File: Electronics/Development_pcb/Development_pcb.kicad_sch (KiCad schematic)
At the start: 11 parts, among them J1 TF-Luna, J2 Pan, J3 Tilt, J4 MP3, Q1 NPN, U1 ESP32-S3-DEVKIT:C-1-N16R8, U2 MP3-TF-16P

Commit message: Refactor code structure for improved readability and maintainability
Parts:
- added D1: 1N5822, Diode_THT:D_DO-201AD_P15.24mm_Horizontal, symbol Diode:1N5822
- added J5: Display, symbol Connector:Conn_01x08_Pin
- added J6: LAZER, symbol Connector:Conn_01x02_Pin
- added J7: Screw_Terminal_01x02, symbol Connector:Screw_Terminal_01x02
- Q1: value NPN -> 2N2222A
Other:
- moved on the sheet: C1, C2, R1, R2

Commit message: Refactor code structure for improved readability and maintainability
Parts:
- removed D1: 1N5822, Diode_THT:D_DO-201AD_P15.24mm_Horizontal, symbol Diode:1N5822
- removed J7: Screw_Terminal_01x02, symbol Connector:Screw_Terminal_01x02
- added SW1: SW_SPST, Connector_PinHeader_2.54mm:PinHeader_1x02_P2.54mm_Vertical, symbol Switch:SW_SPST
- C1, C2: footprint (none) -> Capacitor_THT:CP_Radial_D10.0mm_P5.00mm
- J1: footprint (none) -> Connector_PinHeader_2.54mm:PinHeader_1x04_P2.54mm_Vertical
- J2, J3: footprint (none) -> Connector_PinHeader_2.54mm:PinHeader_1x03_P2.54mm_Vertical
- J4, J6: footprint (none) -> Connector_PinHeader_2.54mm:PinHeader_1x02_P2.54mm_Vertical
- J5: footprint (none) -> Connector_PinHeader_2.54mm:PinHeader_1x08_P2.54mm_Vertical
- Q1: footprint (none) -> Package_TO_SOT_THT:TO-92_Inline
- R1, R2: footprint (none) -> Resistor_THT:R_Axial_DIN0207_L6.3mm_D2.5mm_P7.62mm_Horizontal
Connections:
- net +5V: now also C1.1, C2.1, J1.4 (Pin_4), J2.2 (Pin_2), J3.2 (Pin_2), U1.J1_21 (5V0), U2.P$1 (VCC), SW1.2 (B)
- net GND: now also C1.2, C2.2, J1.1 (Pin_1), J2.3 (Pin_3), J3.1 (Pin_1), J5.1 (Pin_1), Q1.3 (E), U1.J3_1 (GND), U2.P$10 (GND2)
- net at Q1.1 (C): now also J6.1 (Pin_1)
- net at Q1.2 (B): now also R1.1
- net at R1.2: now also U1.J1_6 (GPIO6)
- net +3.3V: now reaches J5.2 (Pin_2)
- net +3.3V: now also J5.8 (Pin_8)
- net at J5.3 (Pin_3): now also U1.J1_8 (GPIO15)
- net at J5.4 (Pin_4): now also U1.J1_15 (GPIO9)
- net at J5.5 (Pin_5): now also U1.J1_16 (GPIO10)
- net at J5.6 (Pin_6): now also U1.J1_17 (GPIO11)
- net at J5.7 (Pin_7): now also U1.J1_18 (GPIO12)
- net at J2.1 (Pin_1): now also U1.J1_4 (GPIO4)
- net at J4.1 (Pin_1): now also U2.P$6 (SPK2)
- net at J4.2 (Pin_2): now also U2.P$8 (SPK1)
- net at U2.P$2 (RX): now also R2.1
- net at U2.P$3 (TX): now also U1.J1_19 (GPIO13)
- net at J6.2 (Pin_2): now also SW1.1 (A)
- net at U1.J1_10 (GPIO17): now also J1.2 (Pin_2)
- net at U1.J1_11 (GPIO18): now also J1.3 (Pin_3)
- net at U1.J1_20 (GPIO14): now also R2.2
- net at U1.J1_5 (GPIO5): now also J3.3 (Pin_3)
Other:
- company: (none) -> Artyom Kiselhof
- title: (none) -> MISA_PCB
- moved on the sheet: C1, C2, R1, R2

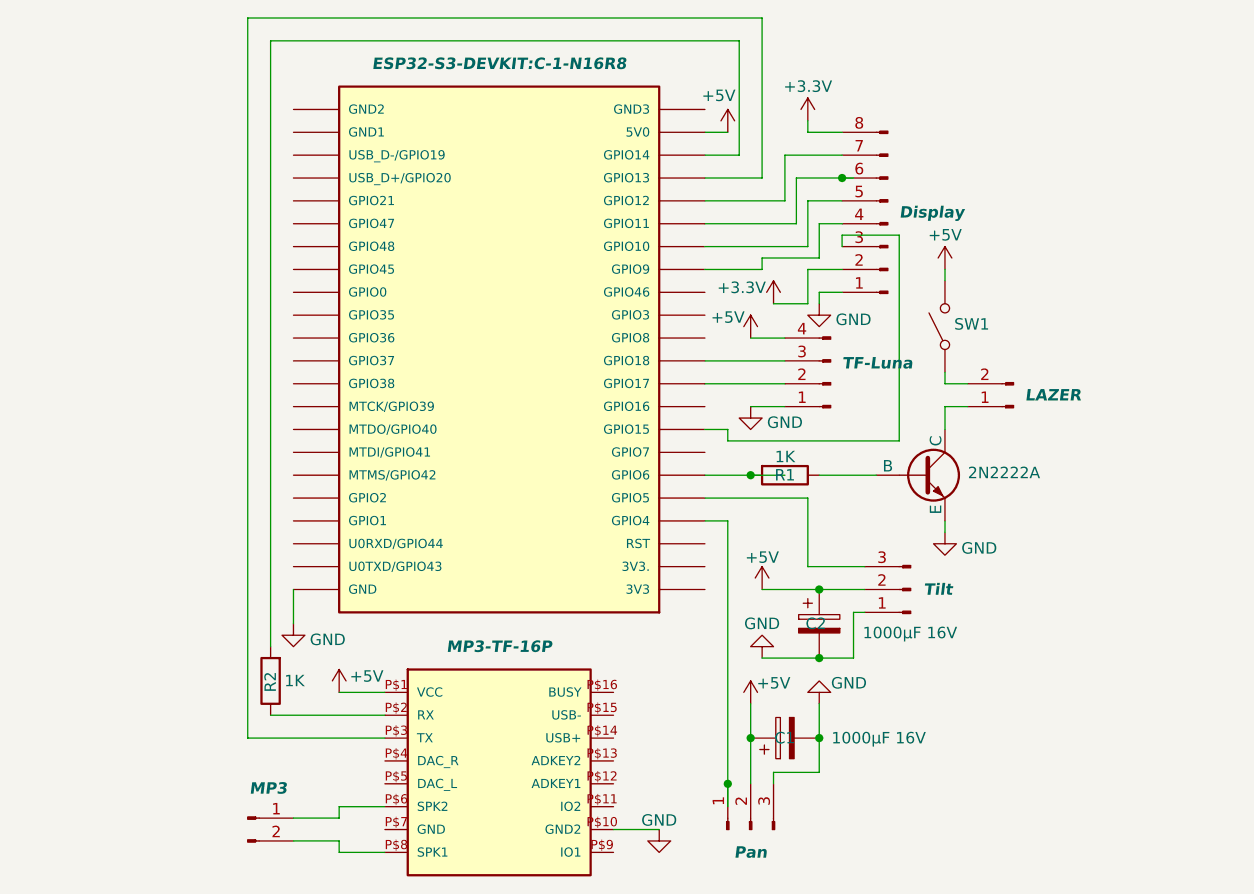
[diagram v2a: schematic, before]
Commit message: Add .DS_Store files and ERC report for Development PCB
- Created .DS_Store files in Electronics and Electronics/Development_pcb directories to store custom Finder attributes.
- Added ERC report (ERC.rpt) for the Development PCB, highlighting errors related to unconnected power pins and pin type mismatches.
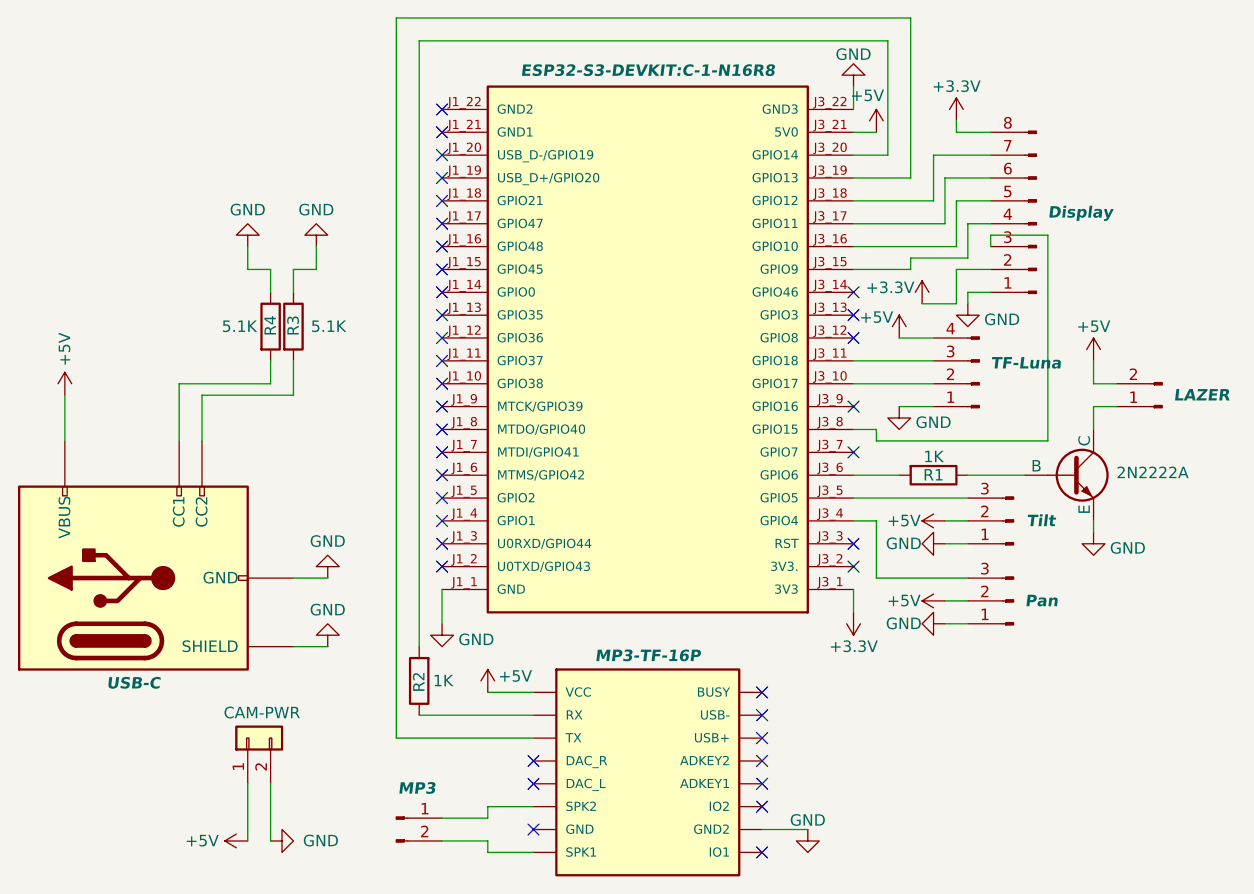
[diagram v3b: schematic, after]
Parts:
- removed C1, C2: 1000µF 16V, Capacitor_THT:CP_Radial_D10.0mm_P5.00mm, symbol Device:C_Polarized
- removed SW1: SW_SPST, Connector_PinHeader_2.54mm:PinHeader_1x02_P2.54mm_Vertical, symbol Switch:SW_SPST
- added J7: CAM-PWR, Connector_PinHeader_2.54mm:PinHeader_1x02_P2.54mm_Vertical, symbol Connector_Generic:Conn_01x02
- added J8: USB-C, Connector_USB:USB_C_Receptacle_HRO_TYPE-C-31-M-12, symbol Connector:USB_C_Receptacle_PowerOnly_6P
- added R3, R4: 5.1K, Resistor_THT:R_Axial_DIN0207_L6.3mm_D2.5mm_P7.62mm_Horizontal, symbol Device:R
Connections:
- net +3.3V: now also U1.J3_1 (3V3)
- net +5V: now also J6.2 (Pin_2), U1.J3_21 (5V0), J7.1 (Pin_1), J8.A9 (VBUS), J8.B9 (VBUS); no longer U1.J1_21 (5V0)
- net GND: now also J2.1 (Pin_1), U1.J1_1 (GND), U1.J3_22 (GND3), J7.2 (Pin_2), J8.A12 (GND), J8.B12 (GND), J8.SH (SHIELD), R3.1, R4.1; no longer J2.3 (Pin_3), U1.J3_1 (GND)
- net at R1.2: now also U1.J3_6 (GPIO6); no longer U1.J1_6 (GPIO6)
- net at J5.3 (Pin_3): now also U1.J3_8 (GPIO15); no longer U1.J1_8 (GPIO15)
- net at J5.4 (Pin_4): now also U1.J3_15 (GPIO9); no longer U1.J1_15 (GPIO9)
- net at J5.5 (Pin_5): now also U1.J3_16 (GPIO10); no longer U1.J1_16 (GPIO10)
- net at J5.6 (Pin_6): now also U1.J3_17 (GPIO11); no longer U1.J1_17 (GPIO11)
- net at J5.7 (Pin_7): now also U1.J3_18 (GPIO12); no longer U1.J1_18 (GPIO12)
- net at U1.J1_4 (GPIO1): no longer J2.1 (Pin_1)
- net at U2.P$3 (TX): now also U1.J3_19 (GPIO13); no longer U1.J1_19 (GPIO13)
- net at U1.J1_10 (GPIO38): no longer J1.2 (Pin_2)
- net at U1.J1_11 (GPIO37): no longer J1.3 (Pin_3)
- net at U1.J1_20 (USB_D-/GPIO19): no longer R2.2
- net at U1.J1_5 (GPIO2): no longer J3.3 (Pin_3)
- net at U1.J3_10 (GPIO17): now also J1.2 (Pin_2)
- net at U1.J3_11 (GPIO18): now also J1.3 (Pin_3)
- net at U1.J3_20 (GPIO14): now also R2.2
- net at U1.J3_4 (GPIO4): now also J2.3 (Pin_3)
- net at U1.J3_5 (GPIO5): now also J3.3 (Pin_3)
- new net: J8.A5 (CC1), R4.2
- new net: J8.B5 (CC2), R3.2
- no-connect marks 0 -> 38
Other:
- moved on the sheet: R1, R2

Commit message: changes
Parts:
- removed J1: TF-Luna, Connector_PinHeader_2.54mm:PinHeader_1x04_P2.54mm_Vertical, symbol Connector:Conn_01x04_Pin
- removed J2: Pan, Connector_PinHeader_2.54mm:PinHeader_1x03_P2.54mm_Vertical, symbol Connector:Conn_01x03_Pin
- removed J3: Tilt, Connector_PinHeader_2.54mm:PinHeader_1x03_P2.54mm_Vertical, symbol Connector:Conn_01x03_Pin
- removed J4: MP3, Connector_PinHeader_2.54mm:PinHeader_1x02_P2.54mm_Vertical, symbol Connector:Conn_01x02_Pin
- removed J5: Display, Connector_PinHeader_2.54mm:PinHeader_1x08_P2.54mm_Vertical, symbol Connector:Conn_01x08_Pin
- removed J6: LAZER, Connector_PinHeader_2.54mm:PinHeader_1x02_P2.54mm_Vertical, symbol Connector:Conn_01x02_Pin
- removed J7: CAM-PWR, Connector_PinHeader_2.54mm:PinHeader_1x02_P2.54mm_Vertical, symbol Connector_Generic:Conn_01x02
- removed J8: USB-C, Connector_USB:USB_C_Receptacle_HRO_TYPE-C-31-M-12, symbol Connector:USB_C_Receptacle_PowerOnly_6P
- removed Q1: 2N2222A, Package_TO_SOT_THT:TO-92_Inline, symbol Simulation_SPICE:NPN
- removed R1, R2: 1K, Resistor_THT:R_Axial_DIN0207_L6.3mm_D2.5mm_P7.62mm_Horizontal, symbol Device:R
- removed R3, R4: 5.1K, Resistor_THT:R_Axial_DIN0207_L6.3mm_D2.5mm_P7.62mm_Horizontal, symbol Device:R
- added C1: 1000µF, Capacitor_THT:CP_Radial_D10.0mm_P5.00mm, symbol Device:C_Polarized_Small
- added C2, C5: 100nF, Capacitor_THT:C_Disc_D5.0mm_W2.5mm_P5.00mm, symbol Device:C_Small
- added C3, C4: 470µF, Capacitor_THT:CP_Radial_D8.0mm_P3.50mm, symbol Device:C_Polarized_Small
- added D1: SA5.0A, Diode_THT:D_DO-15_P10.16mm_Horizontal, symbol Device:D_TVS_Small
- added D2: 1N5819, Diode_THT:D_DO-41_SOD81_P10.16mm_Horizontal, symbol Device:D_Schottky_Small
- added F1: Polyfuse, Capacitor_THT:C_Disc_D5.0mm_W2.5mm_P5.00mm, symbol Device:Polyfuse_Small
- added J1: Pan-Servo, Connector_PinHeader_2.54mm:PinHeader_1x03_P2.54mm_Vertical, symbol Connector_Generic:Conn_01x03
- added J2: Tilt-Servo, Connector_PinHeader_2.54mm:PinHeader_1x03_P2.54mm_Vertical, symbol Connector_Generic:Conn_01x03
- added J3: cam-power, Connector_JST:JST_XH_B2B-XH-A_1x02_P2.50mm_Vertical, symbol Connector_Generic:Conn_01x02
- added J4: laser-power, Connector_JST:JST_XH_B2B-XH-A_1x02_P2.50mm_Vertical, symbol Connector_Generic:Conn_01x02
- added J5: SPEAKER, Connector_JST:JST_XH_B2B-XH-A_1x02_P2.50mm_Vertical, symbol Connector_Generic:Conn_01x02
- added J6: TFT_display, Connector_JST:JST_XH_B8B-XH-A_1x08_P2.50mm_Vertical, symbol Connector_Generic:Conn_01x08
- added J7: lidar-TOF, Connector_PinHeader_2.54mm:PinHeader_1x04_P2.54mm_Vertical, symbol Connector_Generic:Conn_01x04
- added J8: USB_C_IN, TerminalBlock_Phoenix:TerminalBlock_Phoenix_MKDS-3-2-5.08_1x02_P5.08mm_Horizontal, symbol Connector:Screw_Terminal_01x02
- added Q1: PN2222A, Package_TO_SOT_THT:TO-92_Inline, symbol Transistor_BJT:Q_NPN_EBC
- added R3: 1k, Resistor_THT:R_Axial_DIN0207_L6.3mm_D2.5mm_P10.16mm_Horizontal, symbol Device:R_Small
- added R4: 1kΩ, Resistor_THT:R_Axial_DIN0207_L6.3mm_D2.5mm_P10.16mm_Horizontal, symbol Device:R_Small
- U1: value ESP32-S3-DEVKIT:C-1-N16R8 -> ESP32-S3-DEVKITC-1-N8R8; footprint ESP32-S3-DEVKITC-1-N8R8:ESP32-S3-DEVKITC-1-N8R8 -> Development_pcb:ESP32-S3-DevKitC-1_Socket; Description_1 The ESP32-S3-DEVKITC-1-N8R8 from Espressif Systems is a dev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 -> (none)
- U2: Description_1 MP3 player module data sheet -> (none)
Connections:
- net +3.3V is gone; now on net GND: U1.J3_1 (GND)
- net +5V: now also C1.1, C2.1, C3.1, C4.1, C5.1, D1.1 (A1), D2.2 (A), F1.2, J1.2 (Pin_2), J2.2 (Pin_2), J3.2 (Pin_2), J4.2 (Pin_2), J7.4 (Pin_4); no longer U1.J3_21 (5V0)
- net GND: now also U1.J1_22 (GND3), U1.J3_21 (GND1), U2.P$7 (GND), C1.2, C2.2, C3.2, C4.2, C5.2, D1.2 (A2), J1.1 (Pin_1), J2.1 (Pin_1), J3.1 (Pin_1), J6.7 (Pin_7), J7.1 (Pin_1), J8.1 (Pin_1), Q1.1 (E); no longer U1.J1_1 (GND)
- net SPK2: now reaches U2.P$6 (SPK2)
- net SPK2: now also J5.2 (Pin_2)
- net SPK1: now reaches U2.P$8 (SPK1)
- net SPK1: now also J5.1 (Pin_1)
- net at U2.P$2 (RX): now also R3.2
- net at U1.J3_19 (USB_D+/GPIO20): no longer U2.P$3 (TX)
- net ESP_TO_LIDAR: now reaches U1.J1_10 (GPIO17)
- net ESP_TO_LIDAR: now also J7.3 (Pin_3)
- net PAN_PWM: now reaches U1.J1_15 (GPIO9)
- net PAN_PWM: now also J1.3 (Pin_3)
- net TILT_PWM: now reaches U1.J1_16 (GPIO10)
- net TILT_PWM: now also J2.3 (Pin_3)
- net DF_RX: now reaches U1.J1_19 (GPIO13)
- net DF_RX: now also R3.1
- net DF_TX: now reaches U1.J1_20 (GPIO14)
- net DF_TX: now also U2.P$3 (TX)
- net at U1.J1_21 (5V0): now also D2.1 (K)
- net TFT_SCK: now reaches U1.J1_4 (GPIO4)
- net TFT_SCK: now also J6.2 (Pin_2)
- net TFT_MOSI: now reaches U1.J1_5 (GPIO5)
- net TFT_MOSI: now also J6.3 (Pin_3)
- net TFT_DC: now reaches U1.J1_6 (GPIO6)
- net TFT_DC: now also J6.4 (Pin_4)
- net TFT_RST: now reaches U1.J1_7 (GPIO7)
- net TFT_RST: now also J6.5 (Pin_5)
- net TFT_CS: now reaches U1.J1_8 (GPIO15)
- net TFT_CS: now also J6.6 (Pin_6)
- net LIDAR_TO_ESP: now reaches U1.J1_9 (GPIO16)
- net LIDAR_TO_ESP: now also J7.2 (Pin_2)
- net LASER_CTRL: now reaches U1.J3_5 (GPIO2)
- net LASER_CTRL: now also R4.1
- new net: Q1.2 (B), R4.2
- new net: F1.1, J8.2 (Pin_2)
- new net: J4.1 (Pin_1), Q1.3 (C)
- new net +3V3: J6.1 (Pin_1), J6.8 (Pin_8), U1.J1_1 (3V3)
- no-connect marks 38 -> 35
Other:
- title: MISA_PCB -> MISA-PCB
